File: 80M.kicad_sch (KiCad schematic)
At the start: 13 parts, among them Q5 MMBT2222A

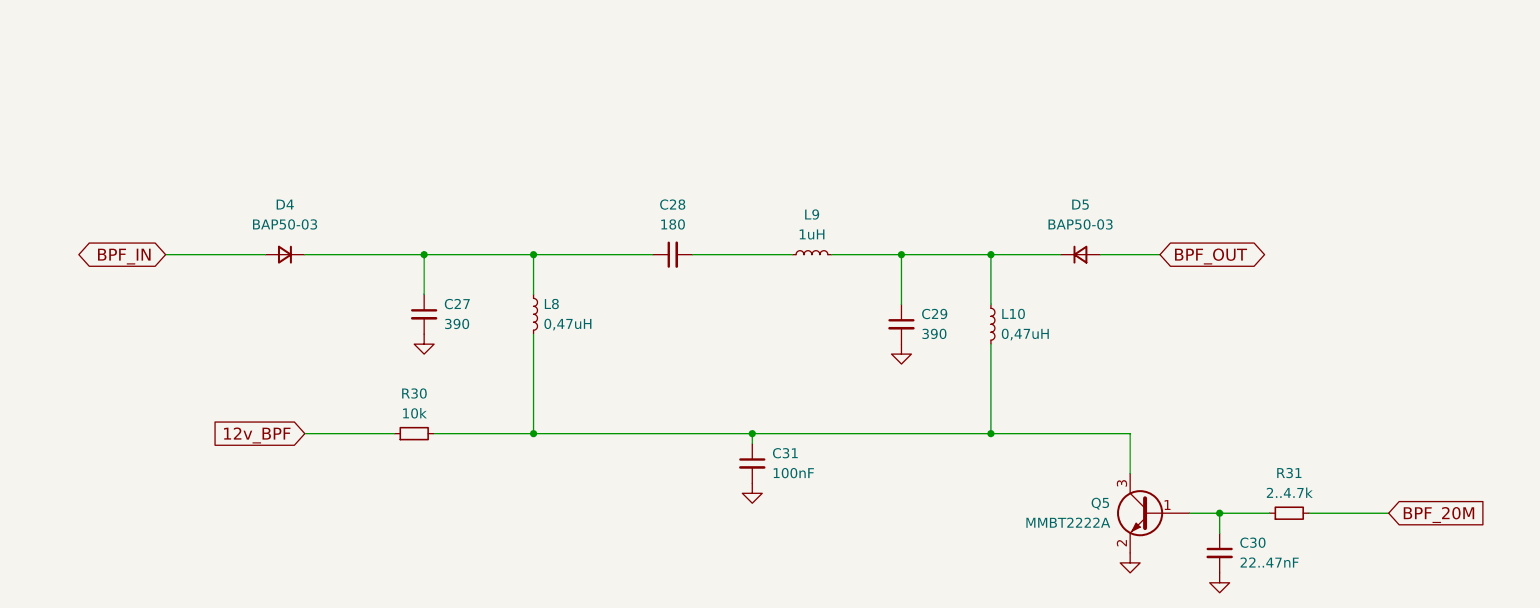
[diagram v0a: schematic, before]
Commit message: add custom footprints, progress on schema and PCB
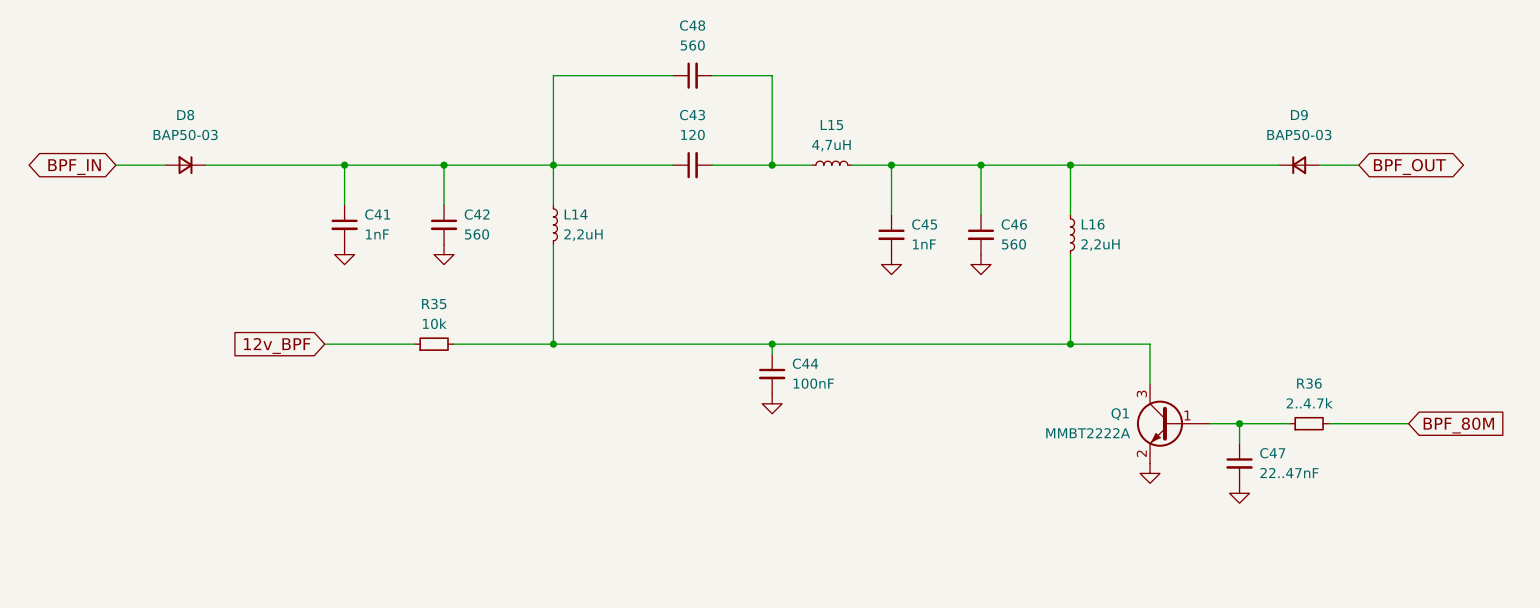
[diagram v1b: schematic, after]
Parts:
- removed C27, C29: 390, SDR_footprints:C_1206_0603, symbol Device:C_Small
- removed C28: 180, SDR_footprints:C_1206_0603, symbol Device:C_Small
- removed C30: 22..47nF, SDR_footprints:C_1206_0603, symbol Device:C_Small
- removed C31: 100nF, SDR_footprints:C_1206_0603, symbol Device:C_Small
- removed D4, D5: BAP50-03, Diode_SMD:D_SOD-323_HandSoldering, symbol Device:D_Small
- removed L10, L8: 0,47uH, SDR_footprints:Resistor_SMD+THTuniversal_0603to2512_RM10_HandSoldering, symbol Device:L_Small
- removed L9: 1uH, SDR_footprints:Resistor_SMD+THTuniversal_0603to2512_RM10_HandSoldering, symbol Device:L_Small
- removed Q5: MMBT2222A, Package_TO_SOT_SMD:SOT-23, symbol Transistor_BJT:MMBT2222A
- removed R30: 10k, SDR_footprints:R_1206_0603, symbol Device:R_Small
- removed R31: 2..4.7k, SDR_footprints:R_1206_0603, symbol Device:R_Small
- added C41, C45: 1nF, Capacitor_SMD:C_0603_1608Metric_Pad1.08x0.95mm_HandSolder, symbol Device:C_Small
- added C42, C46, C48: 560, Capacitor_SMD:C_0603_1608Metric_Pad1.08x0.95mm_HandSolder, symbol Device:C_Small
- added C43: 120, Capacitor_SMD:C_0603_1608Metric_Pad1.08x0.95mm_HandSolder, symbol Device:C_Small
- added C44: 100nF, symbol Device:C_Small
- added C47: 22..47nF, symbol Device:C_Small
- added D8, D9: BAP50-03, Diode_SMD:D_SOD-323_HandSoldering, symbol Device:D_Small
- added L14, L16: 2,2uH, Inductor_THT:L_Axial_L6.6mm_D2.7mm_P10.16mm_Horizontal_Vishay_IM-2, symbol Device:L_Small
- added L15: 4,7uH, Inductor_THT:L_Axial_L6.6mm_D2.7mm_P10.16mm_Horizontal_Vishay_IM-2, symbol Device:L_Small
- added Q1: MMBT2222A, Package_TO_SOT_SMD:SOT-23, symbol Transistor_BJT:MMBT2222A
- added R35: 10k, Resistor_SMD:R_0603_1608Metric_Pad0.98x0.95mm_HandSolder, symbol Device:R_Small
- added R36: 2..4.7k, symbol Device:R_Small
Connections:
- net 12v_BPF: now also R35.1
- net BPF_IN: now also D8.2 (A)
- net BPF_OUT: now also D9.2 (A)
- net GND: now also C41.2, C42.2, C44.2, C45.2, C46.2, C47.2, Q1.2 (E)
- new net: C41.1, C42.1, C43.1, C48.1, D8.1 (K), L14.1
- new net: C47.1, Q1.1 (B), R36.1
- new net: C45.1, C46.1, D9.1 (K), L15.2, L16.1
- new net: C43.2, C48.2, L15.1
- new net: C44.1, L14.2, L16.2, Q1.3 (C), R35.2
- new net BPF_80M: R36.2

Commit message: progress on PCB
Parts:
- C44, C47: footprint (none) -> SDR_footprints:C_1206_0603
- L14, L15, L16: footprint Inductor_THT:L_Axial_L6.6mm_D2.7mm_P10.16mm_Horizontal_Vishay_IM-2 -> SDR_footprints:Resistor_SMD+THTuniversal_0603to2512_RM10_HandSoldering
- R36: footprint (none) -> SDR_footprints:R_1206_0603
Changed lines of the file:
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@@
 			)
 		)
-		(property "Footprint" ""
+		(property "Footprint" "SDR_footprints:R_1206_0603"
 			(at 203.2 102.87 0)
 			(effects
@@
 			)
 		)
-		(property "Footprint" ""
+		(property "Footprint" "SDR_footprints:C_1206_0603"
 			(at 194.31 107.95 0)
 			(effects
@@
 			)
 		)
-		(property "Footprint" "Inductor_THT:L_Axial_L6.6mm_D2.7mm_P10.16mm_Horizontal_Vishay_IM-2"
+		(property "Footprint" "SDR_footprints:Resistor_SMD+THTuniversal_0603to2512_RM10_HandSoldering"
 			(at 106.68 77.47 0)
 			(effects
@@
 			)
 		)
-		(property "Footprint" "Inductor_THT:L_Axial_L6.6mm_D2.7mm_P10.16mm_Horizontal_Vishay_IM-2"
+		(property "Footprint" "SDR_footprints:Resistor_SMD+THTuniversal_0603to2512_RM10_HandSoldering"
 			(at 172.72 78.74 0)
 			(effects
@@
 			)
 		)
-		(property "Footprint" ""
+		(property "Footprint" "SDR_footprints:C_1206_0603"
 			(at 134.62 96.52 0)
 			(effects
@@
 			)
 		)
-		(property "Footprint" "Inductor_THT:L_Axial_L6.6mm_D2.7mm_P10.16mm_Horizontal_Vishay_IM-2"
+		(property "Footprint" "SDR_footprints:Resistor_SMD+THTuniversal_0603to2512_RM10_HandSoldering"
 			(at 142.24 69.85 0)
 			(effects
